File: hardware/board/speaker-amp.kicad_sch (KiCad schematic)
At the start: 9 parts, among them U4 MAX9717x

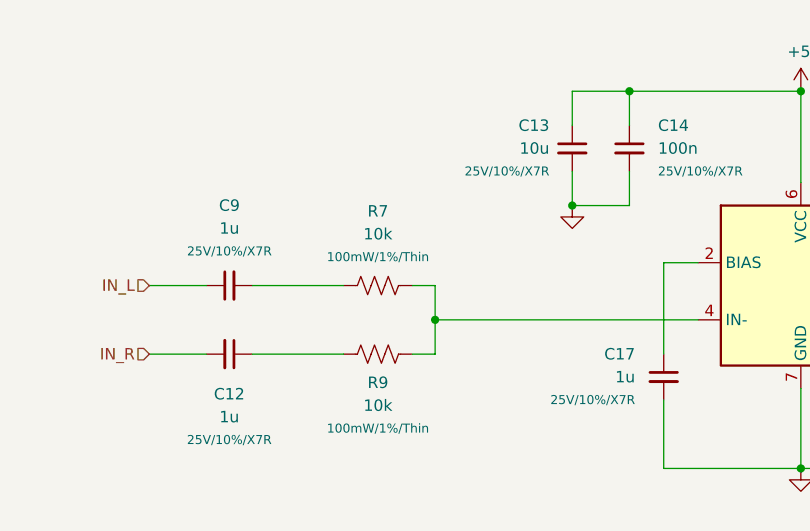
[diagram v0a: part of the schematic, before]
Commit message: Hardware v10:
- Replaced EOL 5V DC-DC converter with new TI part.
- Re-drawn schematic to current Winterbloom standards and style.
- Improved layout and color-coding.
- Updated branding and silk screen.
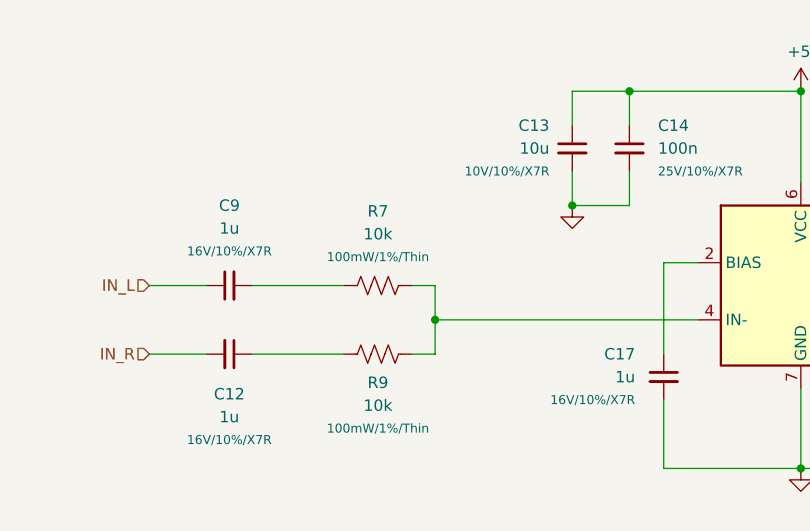
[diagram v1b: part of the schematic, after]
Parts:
- C12, C17, C9: LCSC (none) -> C59782; MPN (none) -> CL10B105KO8NNNC; Notes Bulk cap -> Audio path; Rating 25V/10%/X7R -> 16V/10%/X7R
- C13: LCSC (none) -> C2959727; MPN (none) -> GRM188Z71A106KA73D; Rating 25V/10%/X7R -> 10V/10%/X7R
- C14: LCSC (none) -> C1591; MPN (none) -> CL10B104KB8NNNC; Notes Bulk cap -> Bypass cap
- LS1: MPN (none) -> B2B-XH-A; Notes (none) -> Connects to speaker: CDS-40288; mpn B2B-XH-A -> (none); notes Connects to speaker: CDS-40288 -> (none)
- R7, R9: LCSC 375503 -> C469659; MPN (none) -> RT0603FRE0710KL
- U4: Substitutes Allowed (none) -> No
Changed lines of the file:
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@@
 	(title_block
 		(title "Speak to Me")
-		(date "2024-07-21")
-		(rev "v9")
+		(date "2024-08-28")
+		(rev "v10")
 		(company "Winterbloom")
 		(comment 1 "Alethea Flowers")
@@
 			)
 		)
-		(property "Notes" "Bulk cap"
+		(property "Notes" "Audio path"
 			(at 85.09 113.03 0)
 			(effects
@@
 			)
 		)
-		(property "Rating" "25V/10%/X7R"
+		(property "Rating" "16V/10%/X7R"
 			(at 85.0836 122.555 90)
 			(effects
@@
 			)
 		)
-		(property "MPN" ""
+		(property "MPN" "CL10B105KO8NNNC"
 			(at 85.09 113.03 0)
 			(effects
@@
 			)
 		)
-		(property "LCSC" ""
+		(property "LCSC" "C59782"
 			(at 85.09 113.03 0)
 			(effects
@@
 		)
 		(property "Substitutes Allowed" "Yes"
-			(at 85.09 113.03 0)
-			(effects
-				(font
-					(size 1.27 1.27)
-				)
-				(hide yes)
-			)
-		)
-		(property "search link" ""
 			(at 85.09 113.03 0)
 			(effects
@@
 			)
 		)
-		(property "Rating" "25V/10%/X7R"
+		(property "Rating" "10V/10%/X7R"
 			(at 120.65 92.7163 0)
 			(effects
@@
 			)
 		)
-		(property "MPN" ""
+		(property "MPN" "GRM188Z71A106KA73D"
 			(at 123.19 90.17 0)
 			(effects
@@
 			)
 		)
-		(property "LCSC" ""
+		(property "LCSC" "C2959727"
 			(at 123.19 90.17 0)
 			(effects
@@
 		)
 		(property "Substitutes Allowed" "Yes"
-			(at 123.19 90.17 0)
-			(effects
-				(font
-					(size 1.27 1.27)
-				)
-				(hide yes)
-			)
-		)
-		(property "search link" ""
 			(at 123.19 90.17 0)
 			(effects
@@
 			)
 		)
-		(property "search link" ""
+		(property "Substitutes Allowed" "No"
 			(at 148.59 105.41 0)
 			(effects
@@
 			)
 		)
-		(property "LCSC" "375503"
+		(property "LCSC" "C469659"
 			(at 101.6 105.41 0)
 			(effects
@@
 			)
 		)
-		(property "MPN" ""
-			(at 101.6 105.41 0)
-			(effects
-				(font
-					(size 1.27 1.27)
-				)
-				(hide yes)
-			)
-		)
-		(property "search link" ""
+		(property "MPN" "RT0603FRE0710KL"
 			(at 101.6 105.41 0)
 			(effects
@@
 			)
 		)
-		(property "Notes" "Bulk cap"
+		(property "Notes" "Audio path"
 			(at 85.09 105.41 0)
 			(effects
@@
 			)
 		)
-		(property "Rating" "25V/10%/X7R"
+		(property "Rating" "16V/10%/X7R"
 			(at 85.0963 101.6 90)
 			(effects
@@
 			)
 		)
-		(property "MPN" ""
+		(property "MPN" "CL10B105KO8NNNC"
 			(at 85.09 105.41 0)
 			(effects
@@
 			)
 		)
-		(property "LCSC" ""
+		(property "LCSC" "C59782"
 			(at 85.09 105.41 0)
 			(effects
@@
 		)
 		(property "Substitutes Allowed" "Yes"
-			(at 85.09 105.41 0)
-			(effects
-				(font
-					(size 1.27 1.27)
-				)
-				(hide yes)
-			)
-		)
-		(property "search link" ""
 			(at 85.09 105.41 0)
 			(effects
@@
 			)
 		)
-		(property "LCSC" "375503"
+		(property "LCSC" "C469659"
 			(at 101.6 113.03 0)
 			(effects
@@
 			)
 		)
-		(property "MPN" ""
-			(at 101.6 113.03 0)
-			(effects
-				(font
-					(size 1.27 1.27)
-				)
-				(hide yes)
-			)
-		)
-		(property "search link" ""
+		(property "MPN" "RT0603FRE0710KL"
 			(at 101.6 113.03 0)
 			(effects
@@
 			)
 		)
-		(property "Notes" "Bulk cap"
+		(property "Notes" "Bypass cap"
 			(at 129.54 90.17 0)
 			(effects
@@
 			)
 		)
-		(property "MPN" ""
+		(property "MPN" "CL10B104KB8NNNC"
 			(at 129.54 90.17 0)
 			(effects
@@
 			)
 		)
-		(property "LCSC" ""
+		(property "LCSC" "C1591"
 			(at 129.54 90.17 0)
 			(effects
@@
 		)
 		(property "Substitutes Allowed" "Yes"
-			(at 129.54 90.17 0)
-			(effects
-				(font
-					(size 1.27 1.27)
-				)
-				(hide yes)
-			)
-		)
-		(property "search link" ""
 			(at 129.54 90.17 0)
 			(effects
@@
 			)
 		)
-		(property "mpn" "B2B-XH-A"
+		(property "MPN" "B2B-XH-A"
 			(at 186.69 106.68 0)
 			(effects
@@
 			)
 		)
-		(property "notes" "Connects to speaker: CDS-40288"
-			(at 186.69 106.68 0)
-			(effects
-				(font
-					(size 1.27 1.27)
-				)
-				(hide yes)
-			)
-		)
-		(property "search link" ""
+		(property "Notes" "Connects to speaker: CDS-40288"
 			(at 186.69 106.68 0)
 			(effects
@@
 			)
 		)
-		(property "Notes" "Bulk cap"
+		(property "Notes" "Audio path"
 			(at 133.35 115.57 0)
 			(effects
@@
 			)
 		)
-		(property "Rating" "25V/10%/X7R"
+		(property "Rating" "16V/10%/X7R"
 			(at 130.175 118.1163 0)
 			(effects
@@
 			)
 		)
-		(property "MPN" ""
+		(property "MPN" "CL10B105KO8NNNC"
 			(at 133.35 115.57 0)
 			(effects
@@
 			)
 		)
-		(property "LCSC" ""
+		(property "LCSC" "C59782"
 			(at 133.35 115.57 0)
 			(effects
@@
 			(at 133.35 115.57 0)
 			(effects
-				(font
-					(size 1.27 1.27)
-				)
-				(hide yes)
-			)
-		)
-		(property "search link" ""
-			(at 133.35 115.57 0)
-			(effects
